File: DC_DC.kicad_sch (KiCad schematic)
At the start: 22 parts, among them Q1 Q_NMOS_GDS, U1 UC3845_SOIC8

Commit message: thing
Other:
- moved on the sheet: C1, C2, C3, C4, C5, C6, C7, D1, D2, L1, Q1, R1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

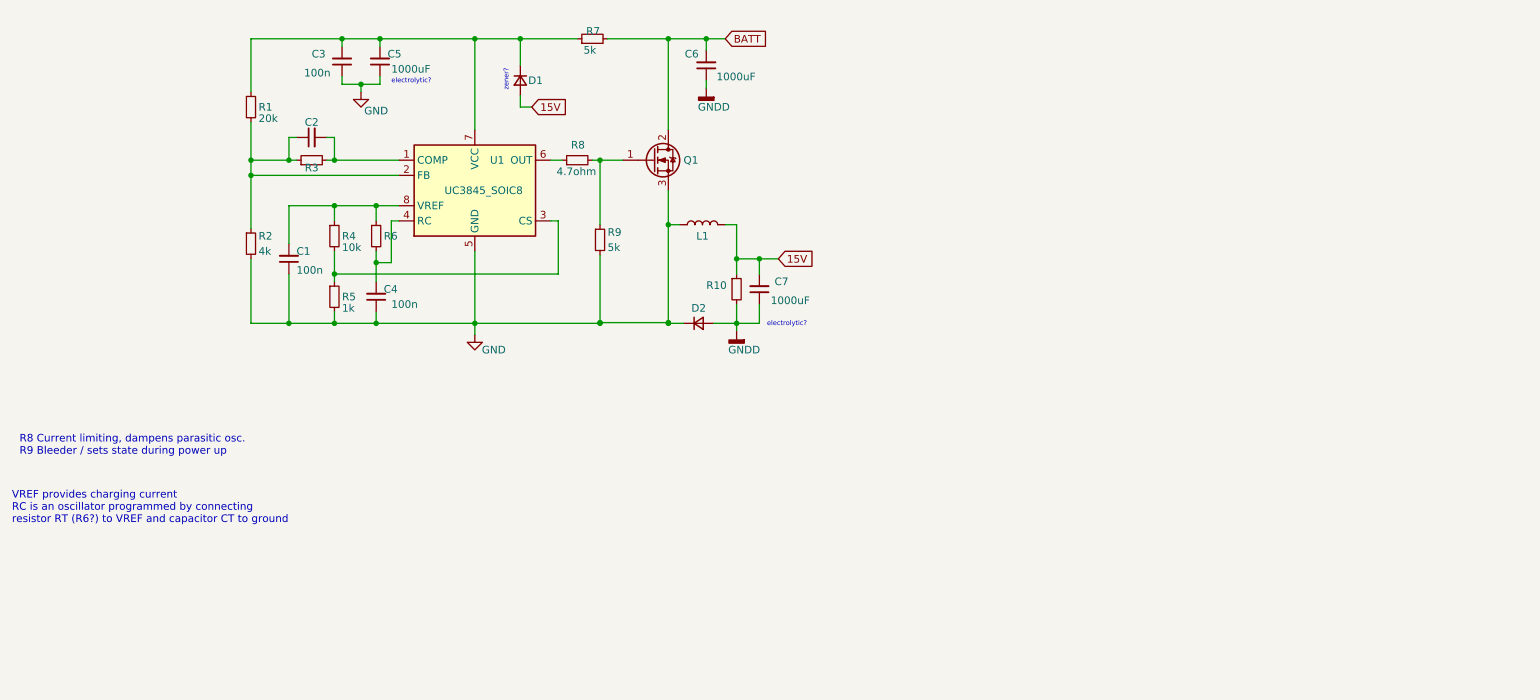
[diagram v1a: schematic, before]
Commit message: DMM commentary work in progress. I do not think the original schematic supplied by Hackey would ever work. TBC
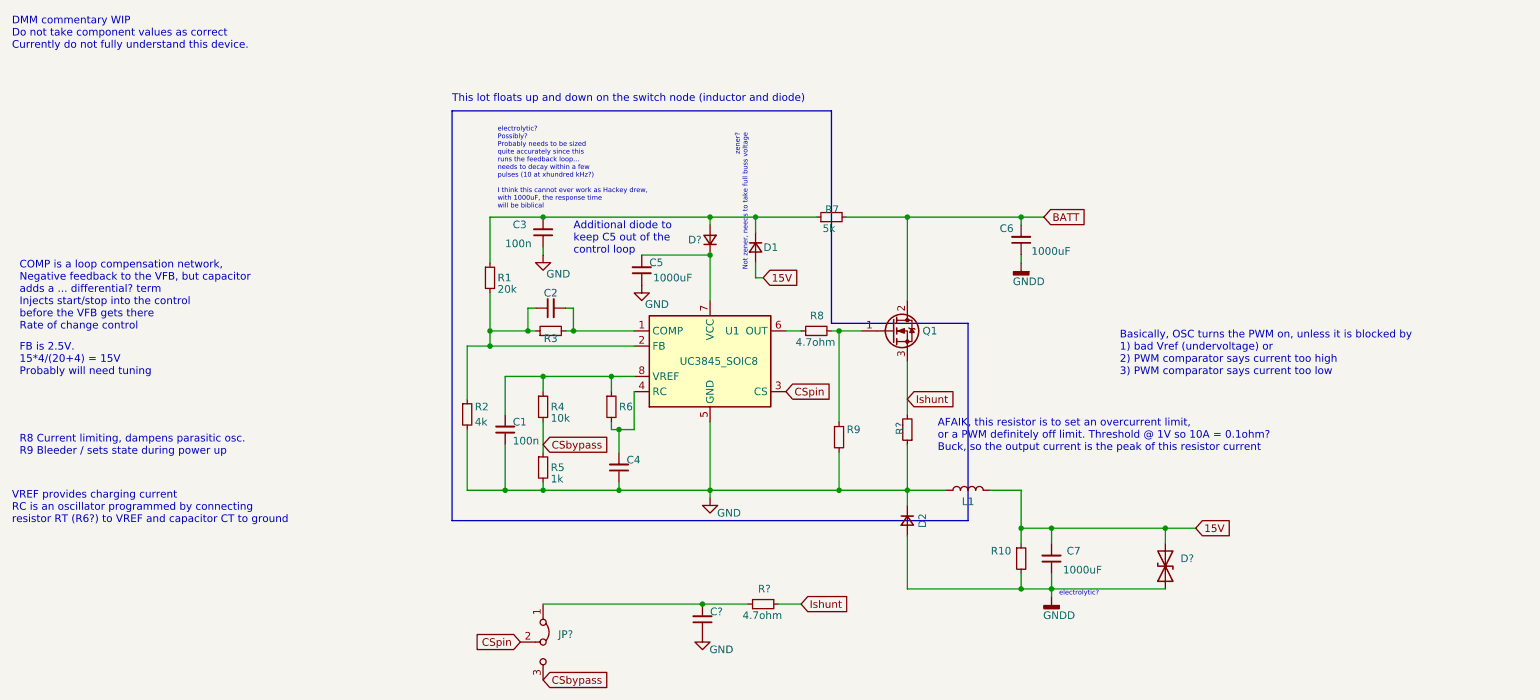
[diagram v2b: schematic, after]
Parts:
- added C?: (no value), symbol Device:C_Small
- added D?: (no value), symbol Device:D_TVS
- added D?: D_Small, symbol Device:D_Small
- added JP?: (no value), symbol Jumper:Jumper_3_Bridged12
- added R?: 4.7ohm, symbol Device:R_Small
- added R?: (no value), symbol Device:R_Small
- C4: value 100n -> (none)
- R10, R6: value R_Small -> (none)
- R9: value 5k -> (none)
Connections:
- net 15V: now also D?.2 (A2)
- net GND: now also D2.1 (K), C?.1, R?.1; no longer Q1.3 (S)
- net GNDD: now also D?.1 (A1)
- net at C3.2, D1.1 (K), R1.1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: now also D?.2 (A); no longer C5.2, U1.7 (VCC)
- net CSbypass: now reaches R4.2, R5.1
- net CSbypass: now also JP?.3 (B); no longer U1.3 (CS)
- new net: C?.2, JP?.1 (A), R?.1
- new net: C5.2, D?.1 (K), U1.7 (VCC)
- new net CSpin: JP?.2 (C), U1.3 (CS)
- new net Ishunt: Q1.3 (S), R?.2, R?.2
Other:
- note added: "AFAIK, this resistor is to set an overcurrent limit, or a PWM definitely off limit. Threshold @ 1V so 10A = 0.1ohm? Buck, so the output current is the peak of this resistor current"
- note added: "Additional diode to keep C5 out of the control loop"
- note added: "Basically, OSC turns the PWM on, unless it is blocked by 1) bad Vref (undervoltage) or 2) PWM comparator says current too high 3) PWM comparator says current too low"
- note added: "COMP is a loop compensation network, Negative feedback to the VFB, but capacitor adds a ... differential? term Injects start/stop into the control before the VFB gets there Rate of change control"
- note added: "DMM commentary WIP Do not take component values as correct Currently do not fully understand this device."
- note added: "FB is 2.5V. 15*4/(20+4) = 15V Probably will need tuning"
- note added: "This lot floats up and down on the switch node (inductor and diode)"
- note added: "electrolytic? Possibly? Probably needs to be sized quite accurately since this runs the feedback loop... needs to decay within a few pulses (10 at xhundred kHz?) I think this cannot ever work as Hackey drew, with 1000uF, the response time will be biblical"
- note added: "zener? Not zener, needs to take full buss voltage"
- note removed: "zener?"
- moved on the sheet: C1, C2, C3, C4, C5, C6, C7, D1, D2, L1, Q1, R1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

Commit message: Mod to make the feedback loop not contain a Vbus 5k pullup
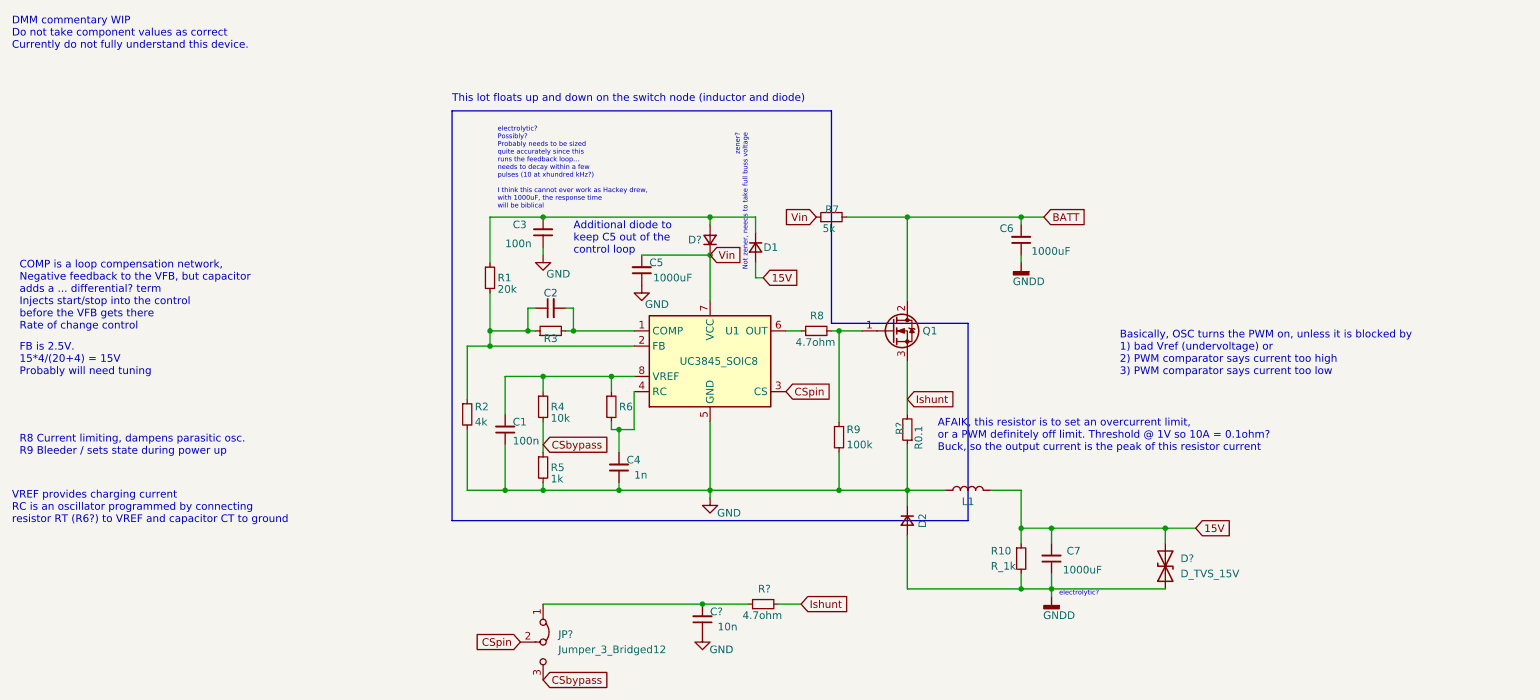
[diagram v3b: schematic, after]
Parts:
- C4: value (none) -> 1n
- C?: value (none) -> 10n
- D?: value (none) -> D_TVS_15V
- JP?: value (none) -> Jumper_3_Bridged12
- R10: value (none) -> R_1k
- R6: value (none) -> R_5k
- R9: value (none) -> 100k
- R?: value (none) -> R0.1
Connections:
- net at C3.2, D1.1 (K), D?.2 (A)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: no longer R7.1
- net Vin: now reaches C5.2, D?.1 (K), U1.7 (VCC)
- net Vin: now also R7.1
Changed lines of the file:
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@@
   (junction (at 153.67 67.31) (diameter 0) (color 0 0 0 0)
   )
-  (junction (at 139.7 48.26) (diameter 0) (color 0 0 0 0)
-  )
   (junction (at 184.15 48.26) (diameter 0) (color 0 0 0 0)
   )
@@
     (stroke (width 0) (type default) (color 0 0 0 0))
   )
-  (wire (pts (xy 139.7 48.26) (xy 149.86 48.26))
-    (stroke (width 0) (type default) (color 0 0 0 0))
-  )
   (wire (pts (xy 179.07 93.98) (xy 184.15 93.98))
     (stroke (width 0) (type default) (color 0 0 0 0))
@@
     (effects (font (size 1.27 1.27)) (justify left bottom))
   )
+  (global_label "Vin" (shape input) (at 132.08 54.61 0) (fields_autoplaced)
+    (effects (font (size 1.27 1.27)) (justify left))
+    (property "Intersheet References" "${INTERSHEET_REFS}" (id 0) (at 137.3355 54.6894 0)
+      (effects (font (size 1.27 1.27)) (justify left) hide)
+    )
+  )
   (global_label "15V" (shape input) (at 213.36 100.33 0) (fields_autoplaced)
     (effects (font (size 1.27 1.27)) (justify left))
@@
     )
   )
+  (global_label "Vin" (shape input) (at 149.86 48.26 180) (fields_autoplaced)
+    (effects (font (size 1.27 1.27)) (justify right))
+    (property "Intersheet References" "${INTERSHEET_REFS}" (id 0) (at 144.6045 48.1806 0)
+      (effects (font (size 1.27 1.27)) (justify right) hide)
+    )
+  )
   (global_label "CSbypass" (shape input) (at 104.14 86.36 0) (fields_autoplaced)
     (effects (font (size 1.27 1.27)) (justify left))
@@
       (effects (font (size 1.27 1.27)) (justify left))
     )
-    (property "Value" "" (id 1) (at 179.07 106.68 0)
+    (property "Value" "R_1k" (id 1) (at 179.07 106.68 0)
       (effects (font (size 1.27 1.27)) (justify left))
     )
@@
       (effects (font (size 1.27 1.27)) (justify left))
     )
-    (property "Value" "" (id 1) (at 106.68 120.6499 90)
+    (property "Value" "Jumper_3_Bridged12" (id 1) (at 106.68 120.6499 90)
       (effects (font (size 1.27 1.27)) (justify left))
     )
@@
       (effects (font (size 1.27 1.27)) (justify right))
     )
-    (property "Value" "" (id 1) (at 210.82 107.9499 90)
+    (property "Value" "D_TVS_15V" (id 1) (at 210.82 107.9499 90)
       (effects (font (size 1.27 1.27)) (justify right))
     )
@@
       (effects (font (size 1.27 1.27)) (justify right))
     )
-    (property "Value" "" (id 1) (at 119.38 91.4335 0)
+    (property "Value" "1n" (id 1) (at 119.38 91.4335 0)
       (effects (font (size 1.27 1.27)) (justify right))
     )
@@
       (effects (font (size 1.27 1.27)) (justify left))
     )
-    (property "Value" "" (id 1) (at 154.94 86.36 0)
+    (property "Value" "100k" (id 1) (at 154.94 86.36 0)
       (effects (font (size 1.27 1.27)) (justify left))
     )
@@
       (effects (font (size 1.27 1.27)) (justify left))
     )
-    (property "Value" "" (id 1) (at 118.11 81.2799 0)
+    (property "Value" "R_5k" (id 1) (at 118.11 81.2799 0)
       (effects (font (size 1.27 1.27)) (justify left) hide)
     )
@@
       (effects (font (size 1.27 1.27)) (justify left))
     )
-    (property "Value" "" (id 1) (at 167.005 83.185 90)
+    (property "Value" "R0.1" (id 1) (at 167.005 83.185 90)
       (effects (font (size 1.27 1.27)) (justify left))
     )
@@
       (effects (font (size 1.27 1.27)) (justify right))
     )
-    (property "Value" "" (id 1) (at 133.35 116.8335 0)
+    (property "Value" "10n" (id 1) (at 133.35 116.8335 0)
       (effects (font (size 1.27 1.27)) (justify right))
     )
